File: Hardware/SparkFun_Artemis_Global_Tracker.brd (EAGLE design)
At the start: 50.8 x 63.5 mm, 219 parts, among them J1 IRIDIUM_9603N, J2 USB-C, J6 U.FL, J7 ANTENNA-GROUNDEDEDGE_SMA, J8 STANDOFFS_M2X0.4_STEEL_6MM, J9 STANDOFFS_M2X0.4_STEEL_6MM, Q1 5.8A/30V/35mΩ, Q2 20V/4.2A/52mΩ/1.4W, Q3 20V/4.2A/52mΩ/1.4W, Q4 600mA/40V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

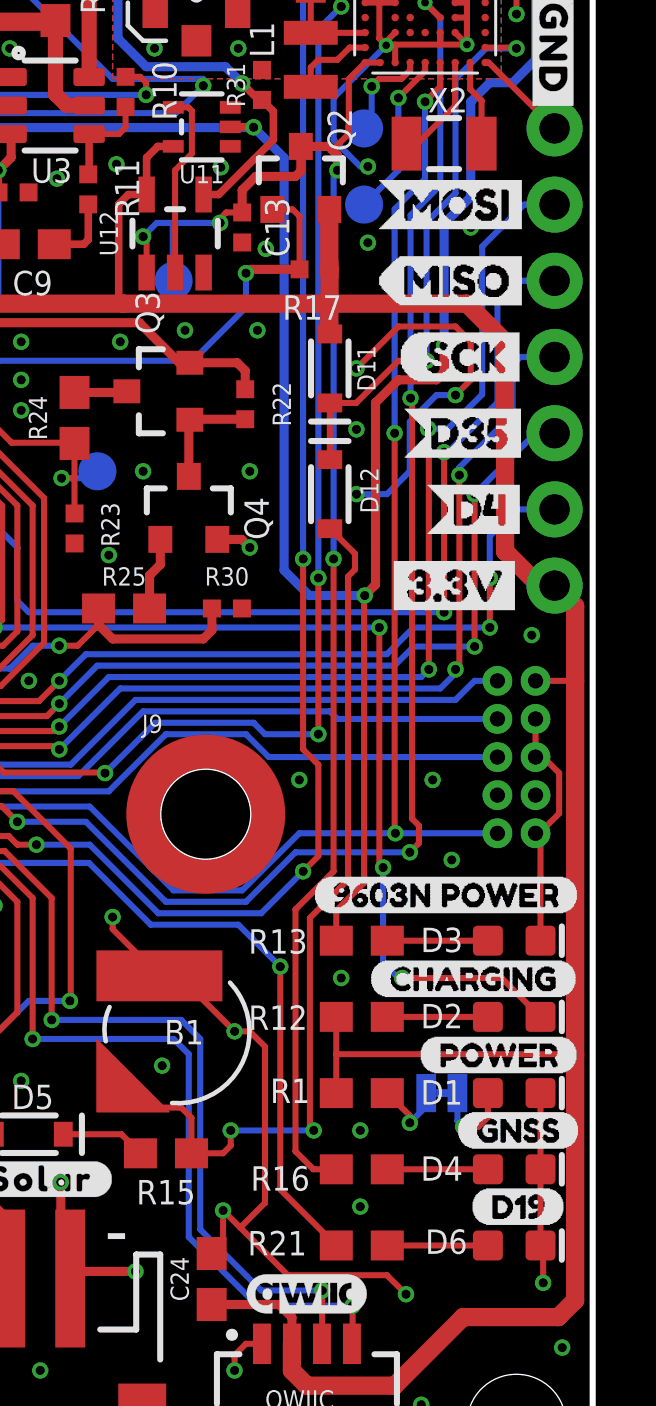
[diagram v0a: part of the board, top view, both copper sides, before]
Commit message: silk updates and R1 to 330 for brighter green power led
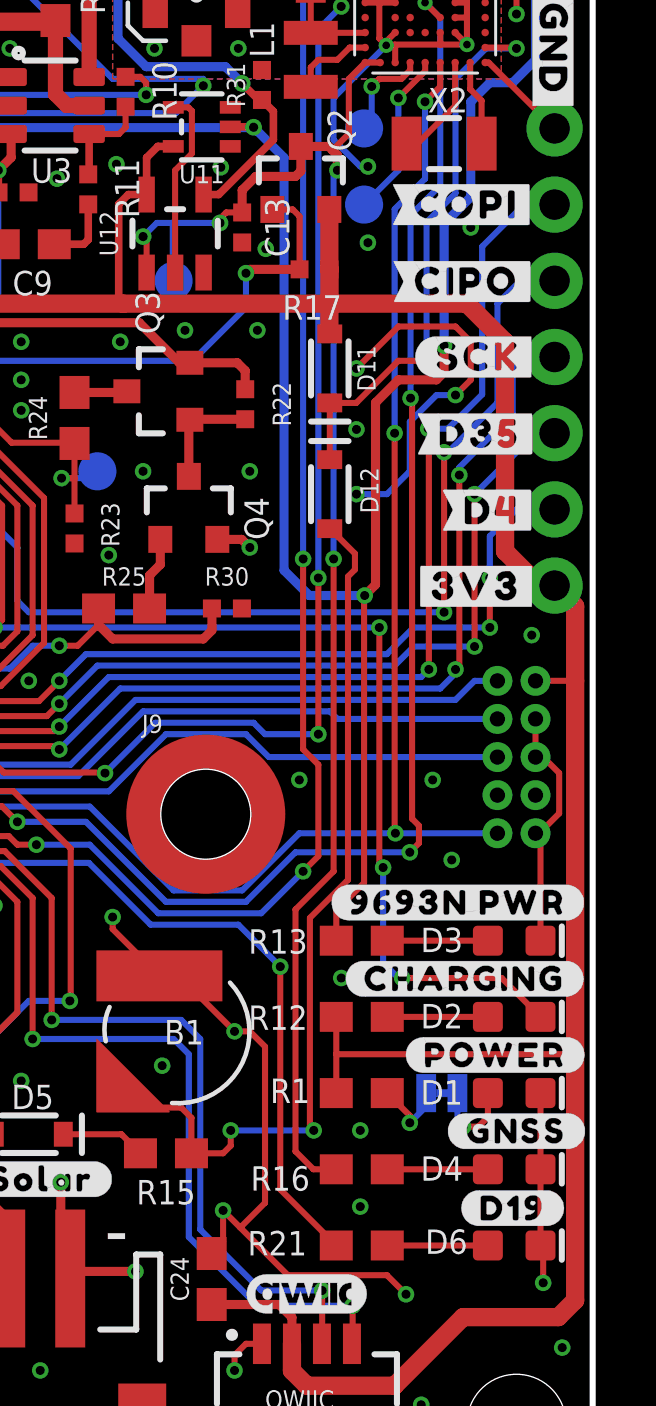
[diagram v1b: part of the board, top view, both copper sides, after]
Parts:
- removed U$24: (no value), Labels-0_04:3#3V2
- removed U$71: (no value), MOSI:MOSI0
- removed U$73: (no value), D4:D40
- added U$29: (no value), output:#D19#0
- added U$59: (no value), output:#CIPO#9695
- added U$60: (no value), output:#SCK#9696
- R1: value 1k -> 330
- U$10: device 9603N_POWER:9603N_POWER0 -> output:#COPI#9694
- U$18: device SCK:SCK0 -> output:#D35#9697
- U$19: device GNSS:GNSS0 -> output:#POWER#21
- U$2: device POWER:POWER0 -> output:#CHARGING#22
- U$50: device D19:D190 -> output:#GNSS#20
- U$68: device D35_m:D350 -> output:#D4#9697
- U$70: device MISO_m:MISO0 -> output:#3V3#153
- U$9: device CHARGING:CHARGING0 -> output:#9693N_PWR#23
- moved U$10 23.6 mm to (46.6, 43.2)
- moved U$70 10.7 mm to (46.9, 30.5)
- moved U$68 3.95 mm to (47.4, 33.0)
- moved U$9 3.89 mm to (46.3, 19.9)
- moved U$18 3.74 mm to (47.0, 35.5)
- moved U$2 2.96 mm to (46.5, 17.4)
- moved U$50 2.94 mm to (48.3, 12.3)
- moved U$19 2.84 mm to (47.5, 14.8)
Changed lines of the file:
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@@
 <element name="JP7" library="SparkFun-Aesthetics" package="FIDUCIAL-1X2" value="FIDUCIAL1X2" x="0.7874" y="62.7126" smashed="yes" rot="MR0"/>
 <element name="JP13" library="SparkFun-Aesthetics" package="FIDUCIAL-1X2" value="FIDUCIAL1X2" x="50.0126" y="0.7874" smashed="yes" rot="MR0"/>
-<element name="R1" library="SparkFun-Resistors" package="0603" value="1k" x="43.1038" y="13.5636" smashed="yes" rot="R180">
+<element name="R1" library="SparkFun-Resistors" package="0603" value="330" x="43.1038" y="13.5636" smashed="yes" rot="R180">
 <attribute name="NAME" x="40.7162" y="13.2334" size="0.8128" layer="25" font="vector" ratio="18" align="bottom-center"/>
-<attribute name="PROD_ID" value="RES-07856" x="43.1038" y="13.5636" size="1.778" layer="27" font="vector" ratio="15" rot="R180" display="off"/>
+<attribute name="PROD_ID" value="RES-00818" x="43.1038" y="13.5636" size="1.778" layer="27" font="vector" ratio="15" rot="R180" display="off"/>
 </element>
 <element name="D1" library="SparkFun-LED" package="LED-0603" value="GREEN" x="48.1838" y="13.5636" smashed="yes">
@@
 <attribute name="PROD_ID" value="CONN-14689" x="22.9032" y="48.46" size="1.778" layer="27" display="off"/>
 </element>
-<element name="U$2" library="POWER" package="POWER0" value="" x="45.0088" y="14.8336" smashed="yes"/>
-<element name="U$9" library="CHARGING" package="CHARGING0" value="" x="43.3578" y="17.3736" smashed="yes"/>
-<element name="U$10" library="9603N_POWER" package="9603N_POWER0" value="" x="41.4528" y="20.1676" smashed="yes"/>
 <element name="U3" library="New_Parts" package="TSOT6" value="ADM4210-1" x="32.7152" y="46.482" smashed="yes" rot="R270">
 <attribute name="NAME" x="32.0772" y="43.91" size="0.8128" layer="25" font="vector" ratio="18"/>
@@
 <element name="VIN/3" library="SparkFun-Connectors" package="PAD.03X.05" value="TEST-POINT3X5" x="34.29" y="34.29" smashed="yes" rot="MR270"/>
 <element name="LOGO4" library="SparkFun-Aesthetics" package="OSHW-LOGO-MINI" value="OSHW-LOGOMINI" x="25.273" y="8.255" smashed="yes" rot="MR0"/>
-<element name="U$24" library="Labels-0_04" package="3#3V2" value="" x="43.688" y="30.48" smashed="yes"/>
 <element name="5V3" library="SparkFun-Connectors" package="PAD.03X.05" value="TEST-POINT3X5" x="27.94" y="48.26" smashed="yes" rot="MR0"/>
-<element name="U$18" library="SCK" package="SCK0" value="" x="44.323" y="38.1" smashed="yes"/>
-<element name="U$19" library="GNSS" package="GNSS0" value="" x="46.228" y="12.319" smashed="yes"/>
-<element name="U$50" library="D19" package="D190" value="" x="46.736" y="9.779" smashed="yes"/>
 <element name="U10" library="SparkFun-IC-Power" package="SOT23-5" value="3.3V" x="5.334" y="33.655" smashed="yes" rot="R270">
 <attribute name="NAME" x="7.493" y="34.544" size="0.6096" layer="25" font="vector" ratio="20" rot="R270"/>
@@
 <attribute name="VOLTAGE" value="2.4V" x="13.97" y="31.242" size="1.778" layer="27" display="off"/>
 </element>
-<element name="U$68" library="D35_m" package="D350" value="" x="44.45" y="35.56" smashed="yes"/>
-<element name="U$70" library="MISO_m" package="MISO0" value="" x="43.561" y="40.64" smashed="yes"/>
-<element name="U$71" library="MOSI" package="MOSI0" value="" x="43.561" y="43.18" smashed="yes"/>
-<element name="U$73" library="D4" package="D40" value="" x="45.212" y="33.02" smashed="yes"/>
 <element name="U$11" library="SparkFun-Aesthetics" package="QWIIC_4MM" value="" x="41.275" y="6.858" smashed="yes"/>
 <element name="U$25" library="SparkFun-Aesthetics" package="QWIIC_5MM" value="" x="41.275" y="1.397" smashed="yes" rot="MR0"/>
@@
 <element name="U$46" library="output" package="#LIPO#164" value="" x="22.1996" y="10.5918" smashed="yes"/>
 <element name="U$45" library="output" package="#SOLAR#165" value="" x="32.4358" y="10.6934" smashed="yes"/>
+<element name="U$29" library="output" package="#D19#0" value="" x="48.133" y="9.7282" smashed="yes"/>
+<element name="U$50" library="output" package="#GNSS#20" value="" x="48.26" y="12.2936" smashed="yes"/>
+<element name="U$19" library="output" package="#POWER#21" value="" x="47.5488" y="14.8336" smashed="yes"/>
+<element name="U$2" library="output" package="#CHARGING#22" value="" x="46.5328" y="17.3736" smashed="yes"/>
+<element name="U$9" library="output" package="#9693N_PWR#23" value="" x="46.3042" y="19.9136" smashed="yes"/>
+<element name="U$10" library="output" package="#COPI#9694" value="" x="46.5836" y="43.18" smashed="yes"/>
+<element name="U$59" library="output" package="#CIPO#9695" value="" x="46.609" y="40.6146" smashed="yes"/>
+<element name="U$60" library="output" package="#SCK#9696" value="" x="46.99" y="38.1" smashed="yes"/>
+<element name="U$18" library="output" package="#D35#9697" value="" x="47.0408" y="35.5346" smashed="yes"/>
+<element name="U$68" library="output" package="#D4#9697" value="" x="47.4472" y="32.9946" smashed="yes"/>
+<element name="U$70" library="output" package="#3V3#153" value="" x="46.9138" y="30.4546" smashed="yes"/>
 </elements>
 <signals>

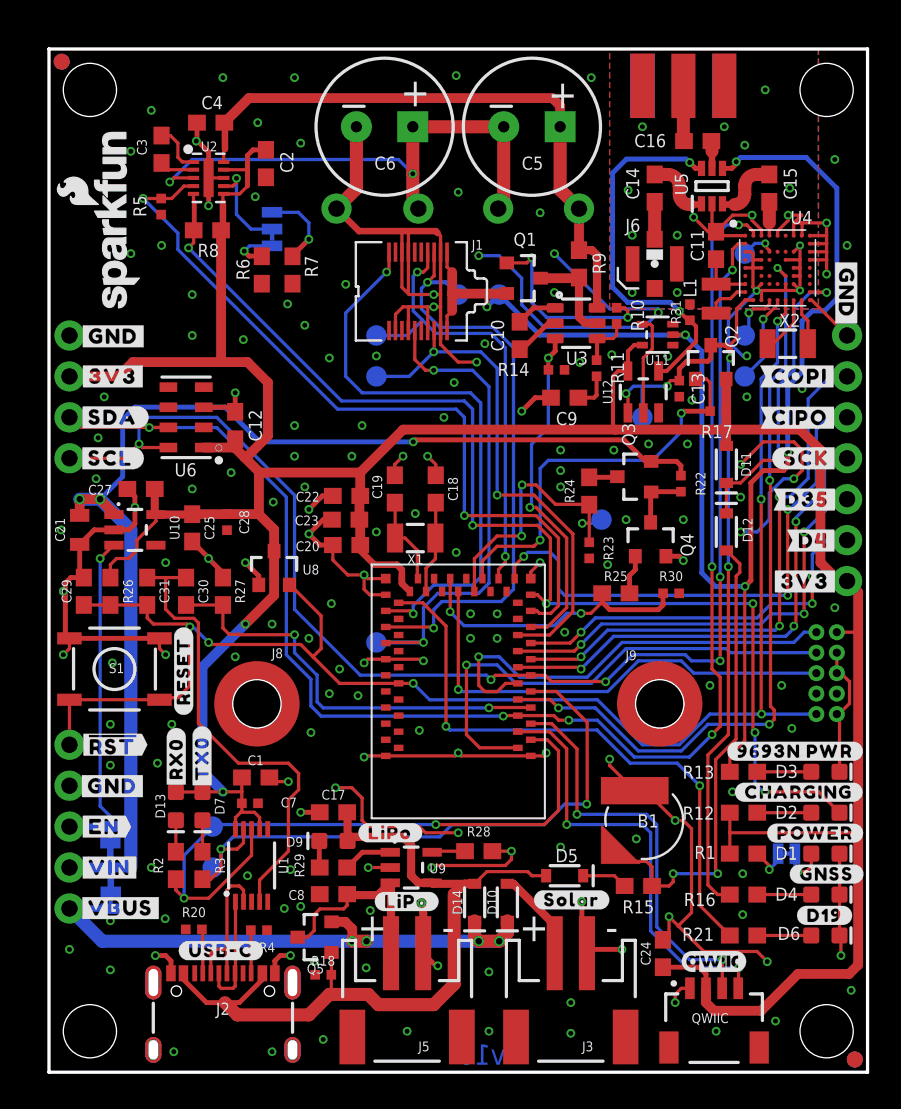
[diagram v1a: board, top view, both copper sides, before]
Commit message: backup battery charge resistor val and switch
-added pch mosfet to switch backup battery charging on and off via GPIO on artemis
-changed backup battery charge source to 3.3V rail, and changed charge resistor to 3.3K
-Moved Iridium module and artemis module down 0.1 inch to allow more clearance around sam-tech connector so epoxy is less likely to flow over/into nearby additional supercap pth pads.
-moved a few other components from 0603 to 0402 to make more room.
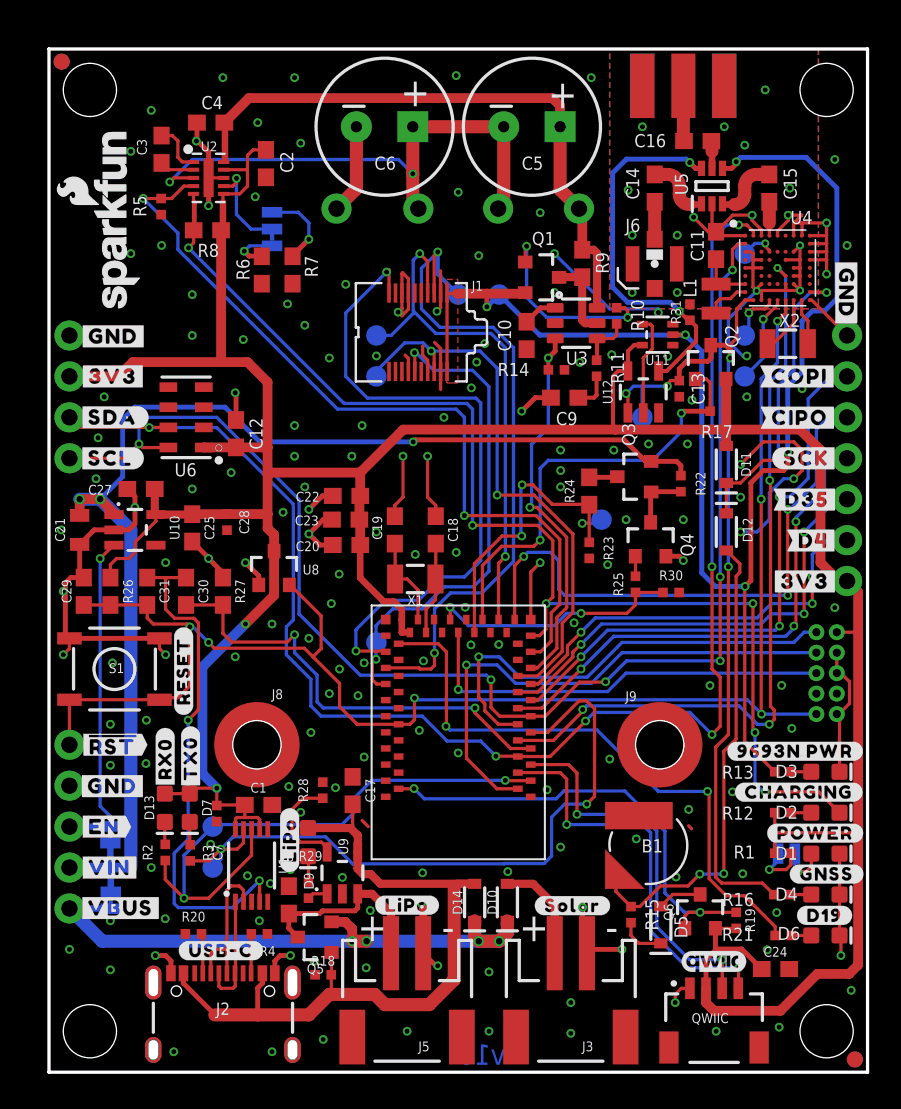
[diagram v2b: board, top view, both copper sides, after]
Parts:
- added Q6: 20V/4.2A/52mΩ/1.4W, SparkFun-DiscreteSemi:SOT23-3
- added R19: 10K, SparkFun-Resistors:0402-TIGHT
- R1, R12, R16, R2, R21, R25, R29, R3: device SparkFun-Resistors:0603 -> SparkFun-Resistors:0402-TIGHT
- R13: value 2.2k -> 2.0K; device SparkFun-Resistors:0603 -> SparkFun-Resistors:0402-TIGHT
- R15: value 62KOHM-0603-1/10W-5% -> 3.3K; device SparkFun-Resistors:0603 -> SparkFun-Resistors:0402-TIGHT
- R28: value 2.0k -> 2.0K; device SparkFun-Resistors:0603 -> SparkFun-Resistors:0402-TIGHT
- moved R28 10.4 mm to (17.0, 17.5), turned to 270 degrees
- moved C24 7.05 mm to (45.1, 6.40), turned to 0 degrees
- moved D5 6.70 mm to (38.0, 9.14), turned to 90 degrees
- moved U$16 6.27 mm to (14.9, 14.4), turned to 90 degrees
- moved U9 4.28 mm to (18.2, 12.4), turned to 0 degrees
- moved C8 2.79 mm to (14.9, 10.7), turned to 90 degrees
- moved C18 2.54 mm to (24.0, 33.7)
- moved C19 2.54 mm to (21.5, 33.7)
- moved J1 2.54 mm to (22.9, 45.9)
- moved J8 2.54 mm to (12.9, 20.3)
- moved J9 2.54 mm to (37.9, 20.3)
- moved U7 2.54 mm to (25.4, 21.6)
- moved X1 2.54 mm to (22.7, 30.6)
- moved R21 2.46 mm to (45.6, 8.48)
- moved R1 2.44 mm to (45.5, 13.6)
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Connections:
- new net ARTEMIS_D44: Q6.1, R19.1, U7.~D44
- new net N$7: D5.A, Q6.3
- net 3.3V: now also Q6.2, R19.2
- net V_USB: no longer D5.A
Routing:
- net GND: track 267.2 -> 172.2 mm, vias 179 -> 178
- net ARTEMIS_D44: track 0.00 -> 28.6 mm, vias 0 -> 2
- net ARTEMIS_D17: track 37.4 -> 42.5 mm
- net ARTEMIS_D18: track 35.9 -> 40.7 mm
- net ARTEMIS_RX0: track 41.1 -> 36.4 mm
- net N$39: track 2.07 -> 6.50 mm
- net ARTEMIS_D25: track 28.7 -> 33.0 mm
- net ARTEMIS_TX0: track 39.6 -> 43.7 mm
- net 3.3V: track 203.0 -> 206.9 mm
- net ARTEMIS_D33: track 29.5 -> 26.3 mm
- net ARTEMIS_D24: track 32.3 -> 35.1 mm
- net V_USB: track 49.5 -> 46.7 mm
- net N$7: track 0.00 -> 2.74 mm
- net ARTEMIS_!RTS!: track 29.5 -> 32.2 mm, vias 0 -> 2
- net ARTEMIS_D6_MISO: track 33.6 -> 36.1 mm
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- added copper zone on layer 1, net EXT_PWR
